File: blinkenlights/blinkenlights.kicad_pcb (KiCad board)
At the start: 4 copper layers, 160 x 100 mm, 113 parts, among them J201 Conn_03x32_Row_Letter_First, J301 Conn_01x01_Female, J302 Conn_01x01_Female, J303 Conn_01x01_Female, SW101 Black, SW102 Orang, SW103 SW_DIP_x01, U101 ATF22V10C, U102 SST39SF020, U103 SST39SF020, U104 74AUC2G07, U105 74AUC2G07, U106 74HC2G14, U301 AP62250Z6, U302 AP62250Z6, U401 74HC244, U402 74AUC2G34

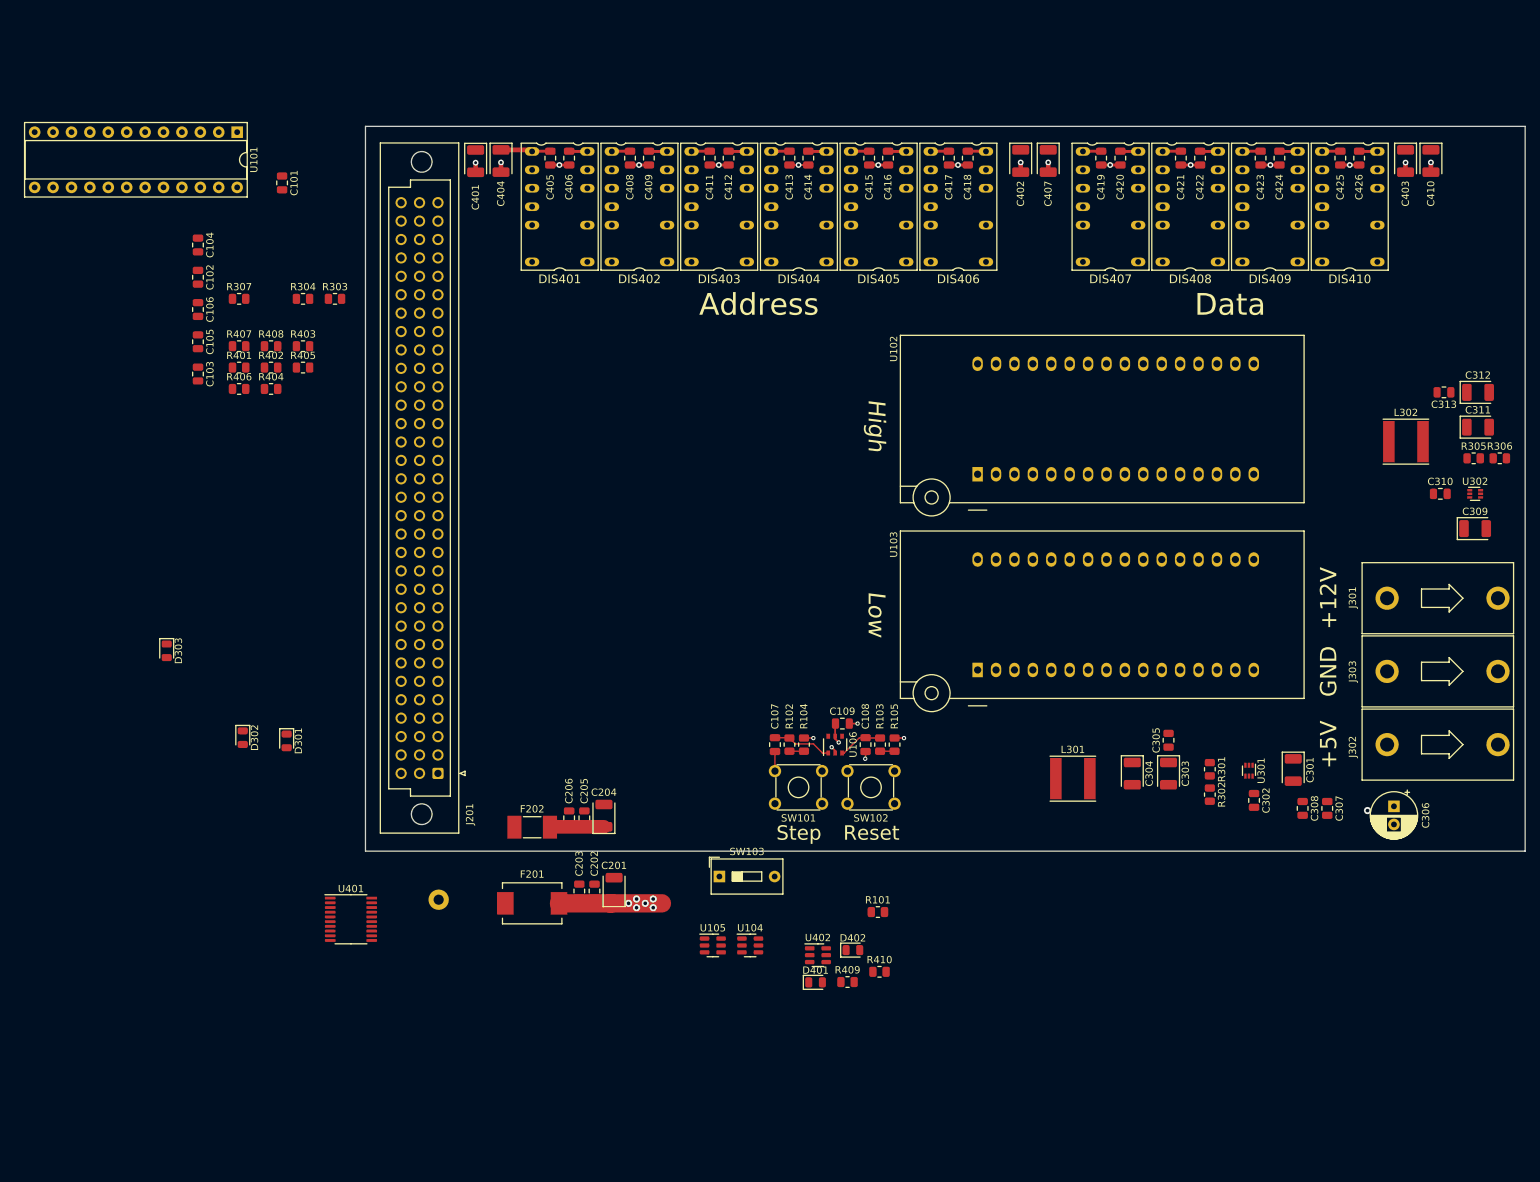
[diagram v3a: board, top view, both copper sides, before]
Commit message: Rework blinkenlights board
- Removed ROMs, GALs and so forth from the blinkenlights board and
  simplified the power distribution significantly. This is in
  preparation for simply placing a big ass microcontroller that allows
  us to perform bus transactions manually (to load bootstrap programs,
  for example) on the system.
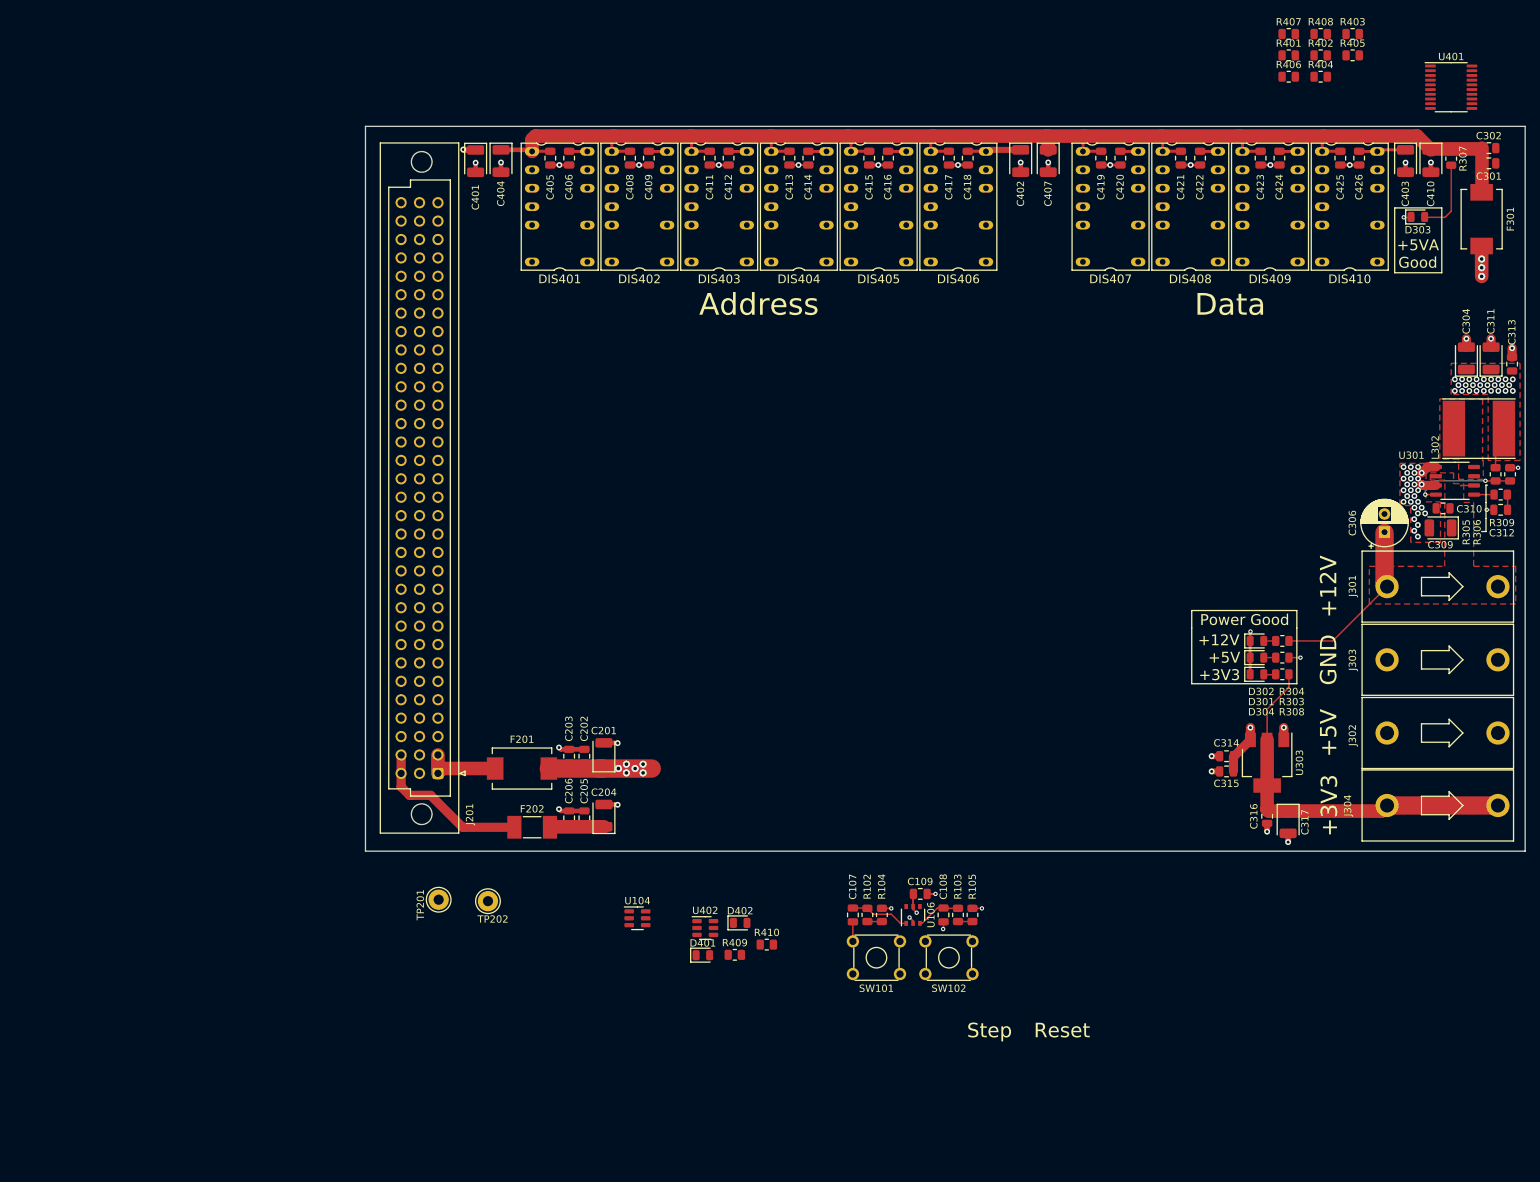
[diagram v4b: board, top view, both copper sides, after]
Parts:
- removed C101, C103, C105: 4.7µF, Capacitor_SMD:C_0805_2012Metric
- removed C102, C104, C106, C305, C308: 100nF, Capacitor_SMD:C_0805_2012Metric
- removed C303: 22µF, Capacitor_Tantalum_SMD:CP_EIA-3528-21_Kemet-B
- removed C307: 1µF, Capacitor_SMD:C_0805_2012Metric
- removed L301: 2.2µH, Inductor_SMD:L_Taiyo-Yuden_NR-60xx
- removed R101, R302: 10k, Resistor_SMD:R_0805_2012Metric
- removed R301: 52k3, Resistor_SMD:R_0805_2012Metric
- removed SW103: SW_DIP_x01, Button_Switch_THT:SW_DIP_SPSTx01_Slide_9.78x4.72mm_W7.62mm_P2.54mm
- removed U101: ATF22V10C, Package_DIP:DIP-24_W7.62mm_Socket
- removed U102, U103: SST39SF020, Socket:DIP_Socket-32_W11.9_W12.7_W15.24_W17.78_W18.5_3M_232-1285-00-0602J
- removed U105: 74AUC2G07, Package_TO_SOT_SMD:SOT-23-6
- removed U302: AP62250Z6, Package_TO_SOT_SMD:SOT-563
- added C314: 4.7µF, Capacitor_SMD:C_0805_2012Metric, F.Cu at (138.8, 106.9)
- added C315: 100nF, Capacitor_SMD:C_0805_2012Metric, F.Cu at (138.8, 109.0)
- added C316: 100nF, Capacitor_SMD:C_0805_2012Metric, F.Cu at (144.4, 115.2)
- added C317: 22µF, Capacitor_Tantalum_SMD:CP_EIA-3528-21_Kemet-B, F.Cu at (147.3, 116.0)
- added D304: Green, LED_SMD:LED_0805_2012Metric, F.Cu at (143.0, 95.6)
- added F301: 1.1A, Fuse:Fuse_Bourns_MF-SM_7.98x5.44mm, F.Cu at (174.0, 32.8)
- added J304: Conn_01x01_Female, 68komputer-common:DELTRON-571-0x00, F.Cu at (178.4, 113.7)
- added R308: 120R, Resistor_SMD:R_0805_2012Metric, F.Cu at (146.5, 95.6)
- added R309: 12k, Resistor_SMD:R_0805_2012Metric, F.Cu at (176.6, 70.8)
- added TP202: TestPoint, TestPoint:TestPoint_Loop_D2.60mm_Drill1.4mm_Beaded, F.Cu at (36.9, 126.9)
- added U303: AMS1117-3.3, Package_TO_SOT_SMD:SOT-223-3_TabPin2, F.Cu at (144.4, 107.8)
- C301: value 10µF -> 100nF; footprint Capacitor_Tantalum_SMD:CP_EIA-3528-21_Kemet-B -> Capacitor_SMD:C_0805_2012Metric
- C302: value 100nF -> 4.7µF
- C312: value 22µF -> 4700pF; footprint Capacitor_Tantalum_SMD:CP_EIA-3528-21_Kemet-B -> Capacitor_SMD:C_0805_2012Metric
- L302: value 2.2µH -> 4.7µH; footprint Inductor_SMD:L_Taiyo-Yuden_NR-60xx -> Inductor_SMD:L_Taiyo-Yuden_NR-80xx_HandSoldering
- R305: value 52k3 -> 4k3
- R306: value 10k -> 820R
- TP201: moved to F.Cu
- U301: value AP62250Z6 -> BD9C301FJ; footprint Package_TO_SOT_SMD:SOT-563 -> Package_SO:SOP-8_3.9x4.9mm_P1.27mm
- moved U401 190.3 mm to (169.8, 14.6)
- moved D303 182.7 mm to (165.2, 32.5), turned to 0 degrees
- moved R307 168.3 mm to (169.8, 24.4), turned to -90 degrees
- moved R401 151.1 mm to (147.4, 10.2)
- moved R402 151.1 mm to (151.8, 10.2)
- moved R403 151.1 mm to (156.2, 7.25)
- moved R404 151.1 mm to (151.8, 13.2)
- moved R405 151.1 mm to (156.2, 10.2)
- moved R406 151.1 mm to (147.4, 13.2)
- moved R407 151.1 mm to (147.4, 7.25)
- moved R408 151.1 mm to (151.8, 7.25)
- moved R304 143.1 mm to (146.5, 91.0), turned to 180 degrees
- moved D302 140.6 mm to (143.0, 91.0), turned to 0 degrees
- moved R303 139.8 mm to (146.5, 93.3), turned to 180 degrees
- moved D301 134.4 mm to (143.0, 93.3), turned to 0 degrees
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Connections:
- C301 pad 1: +12V -> +5VA
- C302 pad 1: Net-(C302-Pad1) -> +5VA
- C302 pad 2: Net-(C302-Pad2) -> GND
- C310 pad 1: Net-(C310-Pad1) -> +12V
- C310 pad 2: Net-(C310-Pad2) -> GND
- C311 pad 1: +5VA -> +5V
- C312 pad 1: +5VA -> GND
- C312 pad 2: GND -> Net-(C312-Pad2)
- C313 pad 1: +5VA -> +5V
- L302 pad 1: Net-(C310-Pad1) -> Net-(L302-Pad1)
- L302 pad 2: +5VA -> +5V
- R305 pad 1: +5VA -> +5V
- U301 pad 1: +12V -> GND
- U301 pad 2: Net-(C302-Pad1) -> +12V
- U301 pad 4: Net-(C302-Pad2) -> Net-(R305-Pad2)
- U301 pad 5: unconnected-(U301-Pad5) -> Net-(U301-Pad5)
- U301 pad 6: Net-(R301-Pad2) -> +12V
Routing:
- net +5VA: track 29.6 -> 191.1 mm
- net +3V3: track 0.00 -> 52.2 mm
- net GND: track 40.0 -> 74.1 mm, vias 19 -> 63
- net +5V: track 45.1 -> 74.6 mm, vias 10 -> 41
- net +12V: track 7.47 -> 33.5 mm
- net Net-(F202-Pad1): track 0.00 -> 22.3 mm
- net Net-(R305-Pad2): track 0.00 -> 14.3 mm, vias 0 -> 2
- net Net-(F201-Pad1): track 0.00 -> 10.6 mm
- net Net-(D303-Pad2): track 0.00 -> 10.3 mm
- net Net-(U301-Pad5): track 0.00 -> 2.76 mm
- net Net-(C312-Pad2): track 0.00 -> 2.12 mm
- net Net-(D304-Pad2): track 0.00 -> 1.65 mm
- net Net-(D302-Pad2): track 0.00 -> 1.65 mm
- net Net-(D301-Pad2): track 0.00 -> 1.65 mm
- added copper zone on F.Cu, net +12V
- added copper zone on F.Cu, net +5V
- added copper zone on F.Cu, net GND
- added copper zone on F.Cu, net Net-(L302-Pad1)
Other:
- board text added: "+3V3"
- board text added: "+5VA Good"
- board text added: "Power Good"
- board text removed: "High"
- board text removed: "Low"

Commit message: Added ATSAM4 CPU to blinkenlights
- This big ol ARM chip is gonna be hooked up to the 68k bus, so that we
  can do bus transactions and (slowly) single step the physical machine.
  This will make bringup simpler and allow programming of the flash
  chips on the CPU board.

- Added a footprint for an USB-C connector (lol)
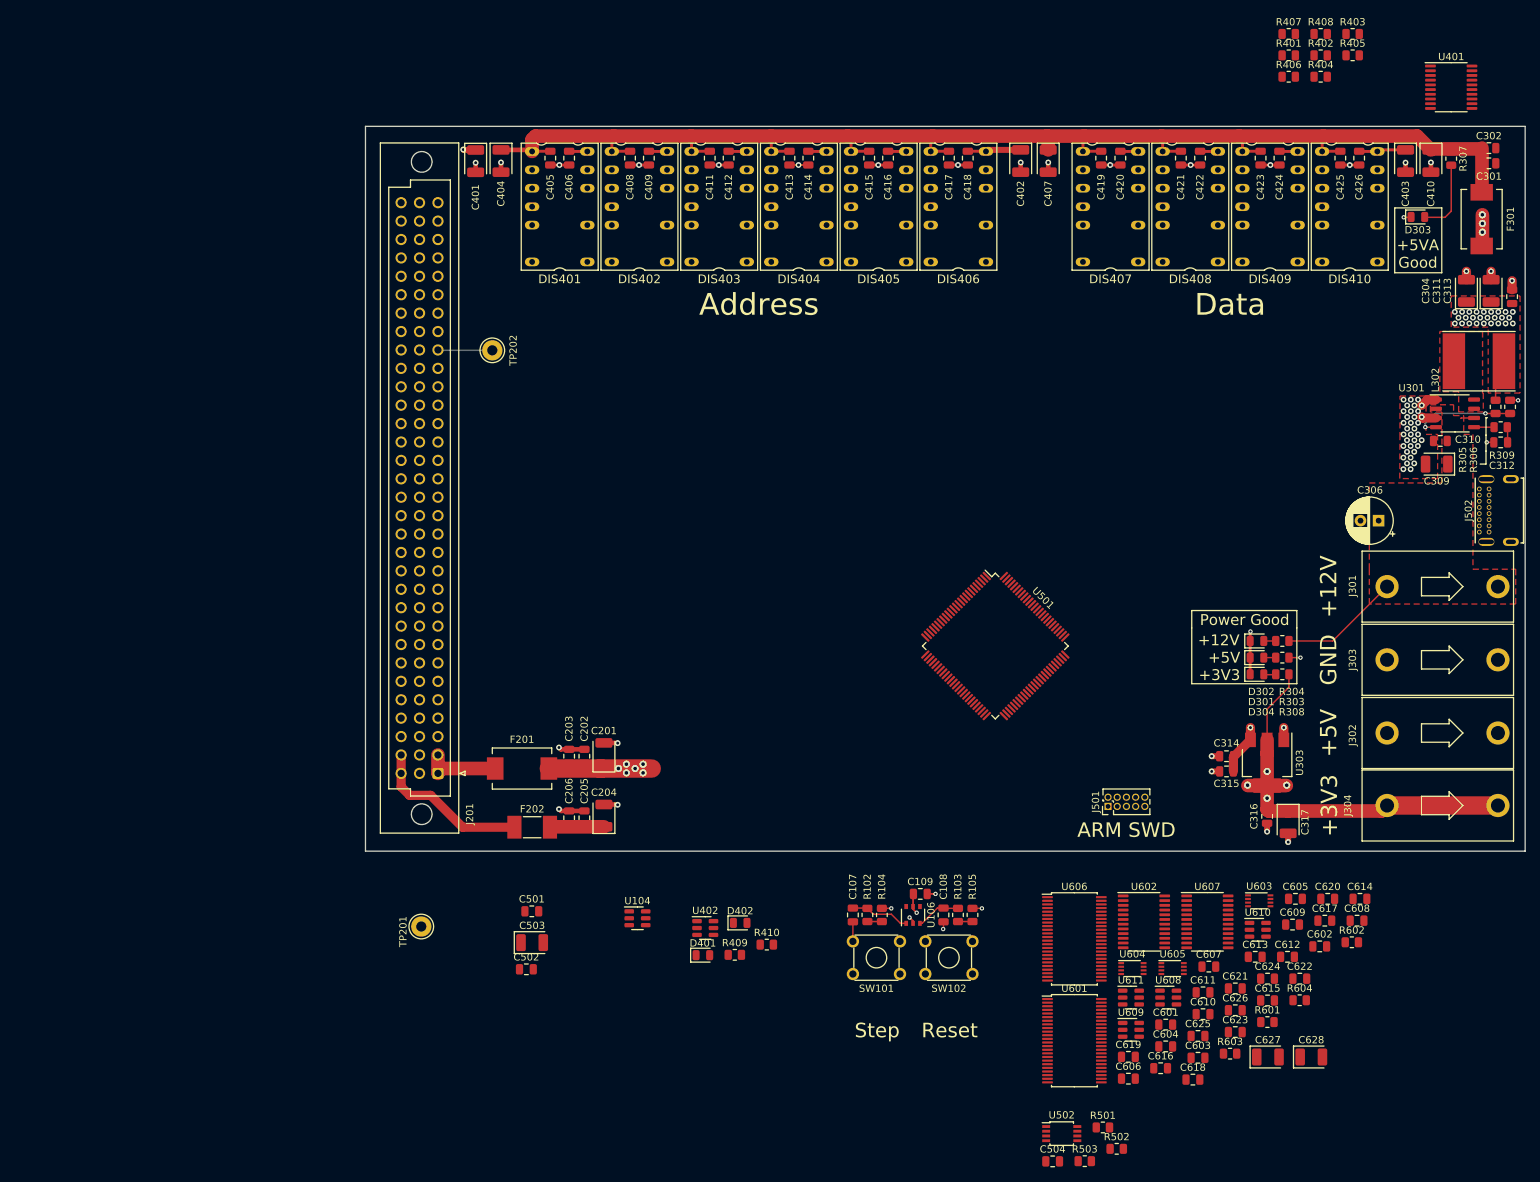
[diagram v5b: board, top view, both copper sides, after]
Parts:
- added C501: 100nF, Capacitor_SMD:C_0805_2012Metric, F.Cu at (43.0, 128.3)
- added C502: 4.7µF, Capacitor_SMD:C_0805_2012Metric, F.Cu at (42.2, 136.3)
- added C503: 10µF, Capacitor_Tantalum_SMD:CP_EIA-3528-21_Kemet-B, F.Cu at (43.0, 132.6)
- added C504: 100nF, Capacitor_SMD:C_0805_2012Metric, F.Cu at (114.8, 162.8)
- added C601: 100nF, Capacitor_SMD:C_0805_2012Metric, F.Cu at (130.4, 143.9)
- added C602: 4.7µF, Capacitor_SMD:C_0805_2012Metric, F.Cu at (151.7, 133.1)
- added C603: 100nF, Capacitor_SMD:C_0805_2012Metric, F.Cu at (134.9, 148.5)
- added C604: 4.7µF, Capacitor_SMD:C_0805_2012Metric, F.Cu at (130.4, 146.9)
- added C605: 100nF, Capacitor_SMD:C_0805_2012Metric, F.Cu at (148.3, 126.6)
- added C606: 4.7µF, Capacitor_SMD:C_0805_2012Metric, F.Cu at (125.3, 151.4)
- added C607: 100nF, Capacitor_SMD:C_0805_2012Metric, F.Cu at (136.4, 135.9)
- added C608: 4.7µF, Capacitor_SMD:C_0805_2012Metric, F.Cu at (156.8, 129.6)
- added C609: 100nF, Capacitor_SMD:C_0805_2012Metric, F.Cu at (147.9, 130.1)
- added C610: 4.7µF, Capacitor_SMD:C_0805_2012Metric, F.Cu at (135.6, 142.5)
- added C611: 100nF, Capacitor_SMD:C_0805_2012Metric, F.Cu at (135.6, 139.5)
- added C612: 4.7µF, Capacitor_SMD:C_0805_2012Metric, F.Cu at (147.2, 134.6)
- added C613: 100nF, Capacitor_SMD:C_0805_2012Metric, F.Cu at (142.8, 134.6)
- added C614: 4.7µF, Capacitor_SMD:C_0805_2012Metric, F.Cu at (157.2, 126.6)
- added C615: 100nF, Capacitor_SMD:C_0805_2012Metric, F.Cu at (144.5, 140.6)
- added C616: 100nF, Capacitor_SMD:C_0805_2012Metric, F.Cu at (129.7, 149.9)
- added C617: 100nF, Capacitor_SMD:C_0805_2012Metric, F.Cu at (152.4, 129.6)
- added C618: 100nF, Capacitor_SMD:C_0805_2012Metric, F.Cu at (134.2, 151.5)
- added C619: 100nF, Capacitor_SMD:C_0805_2012Metric, F.Cu at (125.3, 148.4)
- added C620: 4.7µF, Capacitor_SMD:C_0805_2012Metric, F.Cu at (152.8, 126.6)
- added C621: 100nF, Capacitor_SMD:C_0805_2012Metric, F.Cu at (140.0, 138.9)
- added C622: 4.7µF, Capacitor_SMD:C_0805_2012Metric, F.Cu at (148.9, 137.6)
- added C623: 100nF, Capacitor_SMD:C_0805_2012Metric, F.Cu at (140.0, 145.0)
- added C624: 4.7µF, Capacitor_SMD:C_0805_2012Metric, F.Cu at (144.5, 137.6)
- added C625: 100nF, Capacitor_SMD:C_0805_2012Metric, F.Cu at (134.9, 145.5)
- added C626: 4.7µF, Capacitor_SMD:C_0805_2012Metric, F.Cu at (140.0, 141.9)
- added C627: 10µF, Capacitor_Tantalum_SMD:CP_EIA-3528-21_Kemet-B, F.Cu at (144.5, 148.4)
- added C628: 10µF, Capacitor_Tantalum_SMD:CP_EIA-3528-21_Kemet-B, F.Cu at (150.5, 148.4)
- added J501: Conn_ARM_SWD, Connector_PinHeader_1.27mm:PinHeader_2x05_P1.27mm_Vertical, F.Cu at (122.5, 113.8)
- added J502: USB4085-GF-A_REVA4, 68komputer-common:GCT_USB4085-GF-A_REVA4, F.Cu at (177.7, 73.0)
- added R501: 200k, Resistor_SMD:R_0805_2012Metric, F.Cu at (121.7, 158.1)
- added R502: 10k, Resistor_SMD:R_0805_2012Metric, F.Cu at (123.7, 161.1)
- added R503: 10k, Resistor_SMD:R_0805_2012Metric, F.Cu at (119.2, 162.8)
- added R601: 10k, Resistor_SMD:R_0805_2012Metric, F.Cu at (144.4, 143.6)
- added R602: 10k, Resistor_SMD:R_0805_2012Metric, F.Cu at (156.1, 132.6)
- added R603: 10k, Resistor_SMD:R_0805_2012Metric, F.Cu at (139.3, 147.9)
- added R604: 10k, Resistor_SMD:R_0805_2012Metric, F.Cu at (148.9, 140.6)
- added U501: ATSAM4S8CB-AN, Package_QFP:TQFP-100_14x14mm_P0.5mm, F.Cu at (106.9, 91.7)
- added U502: PCA9306DP, Package_SO:TSSOP-8_3x3mm_P0.65mm, F.Cu at (116.1, 159.0)
- added U601: SN74LVCH16T245, Package_SO:TSSOP-48_6.1x12.5mm_P0.5mm, F.Cu at (117.8, 146.2)
- added U602: SN74LXC8T245, Package_SO:TSSOP-24_4.4x7.8mm_P0.65mm, F.Cu at (127.4, 129.8)
- added U603: SN74LVC2T45, Package_SO:VSSOP-8_2.3x2mm_P0.5mm, F.Cu at (143.3, 126.8)
- added U604: SN74LVC2T45, Package_SO:VSSOP-8_2.3x2mm_P0.5mm, F.Cu at (125.8, 136.2)
- added U605: SN74LVC2T45, Package_SO:VSSOP-8_2.3x2mm_P0.5mm, F.Cu at (131.4, 136.2)
- added U606: SN74LVCH16T245, Package_SO:TSSOP-48_6.1x12.5mm_P0.5mm, F.Cu at (117.8, 132.1)
- added U607: SN74LXC8T245, Package_SO:TSSOP-24_4.4x7.8mm_P0.65mm, F.Cu at (136.2, 129.8)
- added U608: 74LVC2G06, Package_TO_SOT_SMD:SOT-23-6, F.Cu at (130.8, 140.2)
- added U609: 74LVC2G06, Package_TO_SOT_SMD:SOT-23-6, F.Cu at (125.6, 144.7)
- added U610: 74LVC2G06, Package_TO_SOT_SMD:SOT-23-6, F.Cu at (143.1, 130.8)
- added U611: 74LVC2G06, Package_TO_SOT_SMD:SOT-23-6, F.Cu at (125.6, 140.2)
- moved TP202 76.0 mm to (37.5, 50.9), turned to 90 degrees
- moved C310 9.31 mm to (168.3, 63.4)
- moved R309 9.31 mm to (176.6, 61.5)
- moved C304 9.30 mm to (171.9, 42.7)
- moved C311 9.30 mm to (175.3, 42.7)
- moved C312 9.30 mm to (176.6, 63.6)
- moved C313 9.30 mm to (178.2, 43.5)
- moved L302 9.30 mm to (173.6, 52.4)
- moved U301 9.30 mm to (170.3, 59.6)
- moved R305 9.30 mm to (175.9, 58.7)
- moved R306 9.30 mm to (177.9, 58.7)
- moved C309 8.82 mm to (167.8, 66.6)
- moved TP201 4.41 mm to (27.7, 130.4)
- moved C306 1.78 mm to (159.8, 74.4), turned to 180 degrees
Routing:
- net +3V3: track 52.2 -> 60.7 mm, vias 0 -> 4
- net +12V: track 33.5 -> 26.0 mm
- net /CLK: track 0.00 -> 7.52 mm
- net GND: vias 63 -> 69
- added copper zone on In2.Cu, net +3V3
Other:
- board text added: "ARM SWD"

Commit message: removed usb that shit's whack yo
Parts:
- J502: value USB4085-GF-A_REVA4 -> Conn_02x03_Odd_Even; footprint 68komputer-common:GCT_USB4085-GF-A_REVA4 -> Connector_PinHeader_2.54mm:PinHeader_2x03_P2.54mm_Vertical
- moved J502 75.8 mm to (112.6, 111.9), turned to -90 degrees
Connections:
- U501 pad 44: unconnected-(U501-Pad44) -> /Microcontroller/UART_TXD
- U501 pad 46: unconnected-(U501-Pad46) -> /Microcontroller/UART_RXD
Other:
- board text added: "ARM TTY"
